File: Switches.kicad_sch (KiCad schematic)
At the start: 114 parts, among them SW1 Esc, SW10 F9, SW100 RightGUI, SW101 App, SW102 RCtrl, SW103 LeftArr, SW104 DownArr, SW105 RightArr, SW106 NP0, SW107 NP., SW108 LCtrl, SW109 LeftGUI, SW11 F10, SW110 Alt, SW111 Space, SW112 Alt Gr, SW113 App, SW114 RCtrl, SW12 F11, SW13 F12, SW14 PrtSc, SW15 ScrLck, SW16 Pause, SW17 `, SW18 1, SW19 2, SW2 F1, SW20 3, SW21 4, SW22 5, SW23 6, SW24 7, SW25 8, SW26 9, SW27 0, SW28 -, SW29 =, SW3 F2, SW30 Bkspc, SW31 Insert, SW32 Home, SW33 PgUp, SW34 NumLck, SW35 NP/, SW36 NP*, SW37 NP-, SW38 Tab, SW39 Q, SW4 F3, SW40 W, SW41 E, SW42 R, SW43 T, SW44 Y, SW45 U, SW46 I, SW47 O, SW48 P, SW49 [, SW5 F4, SW50 ], SW51 ANSI \, SW52 Delete, SW53 End, SW54 PgDn, SW55 NP7, SW56 NP8, SW57 NP9, SW58 NP+, SW59 Caps, SW6 F5, SW60 A, SW61 S, SW62 D, SW63 F, SW64 G, SW65 H, SW66 J, SW67 K, SW68 L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

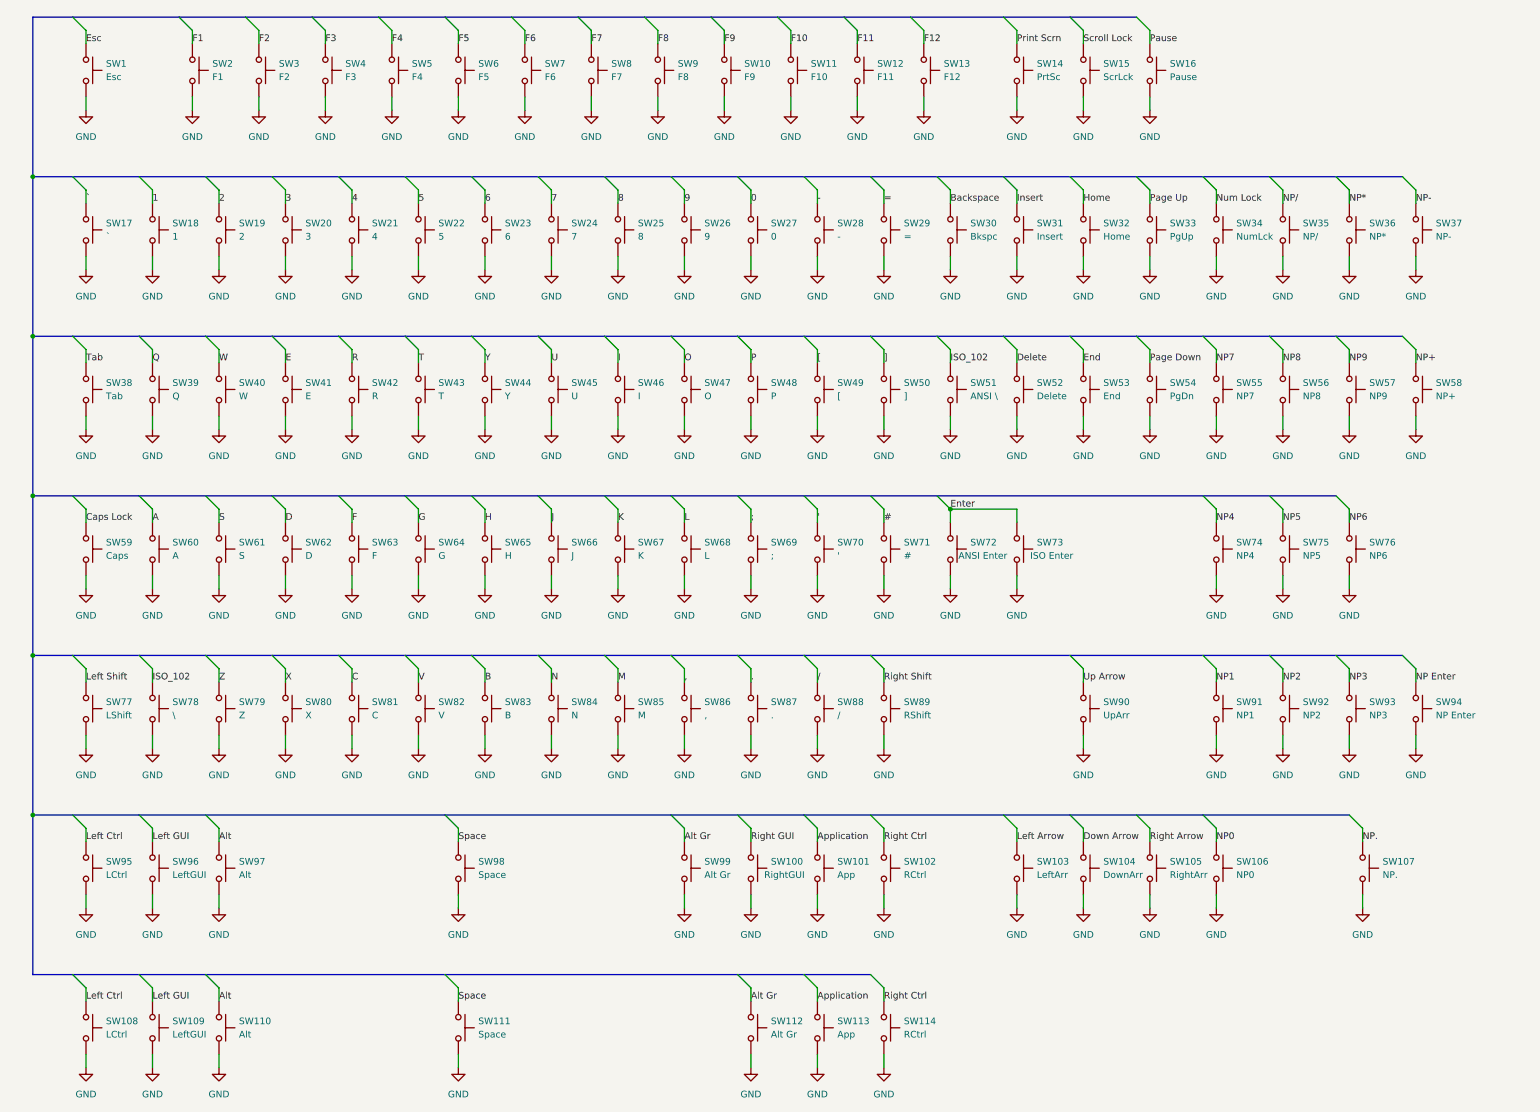
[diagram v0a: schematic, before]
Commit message: updates to board-to-board connector placement
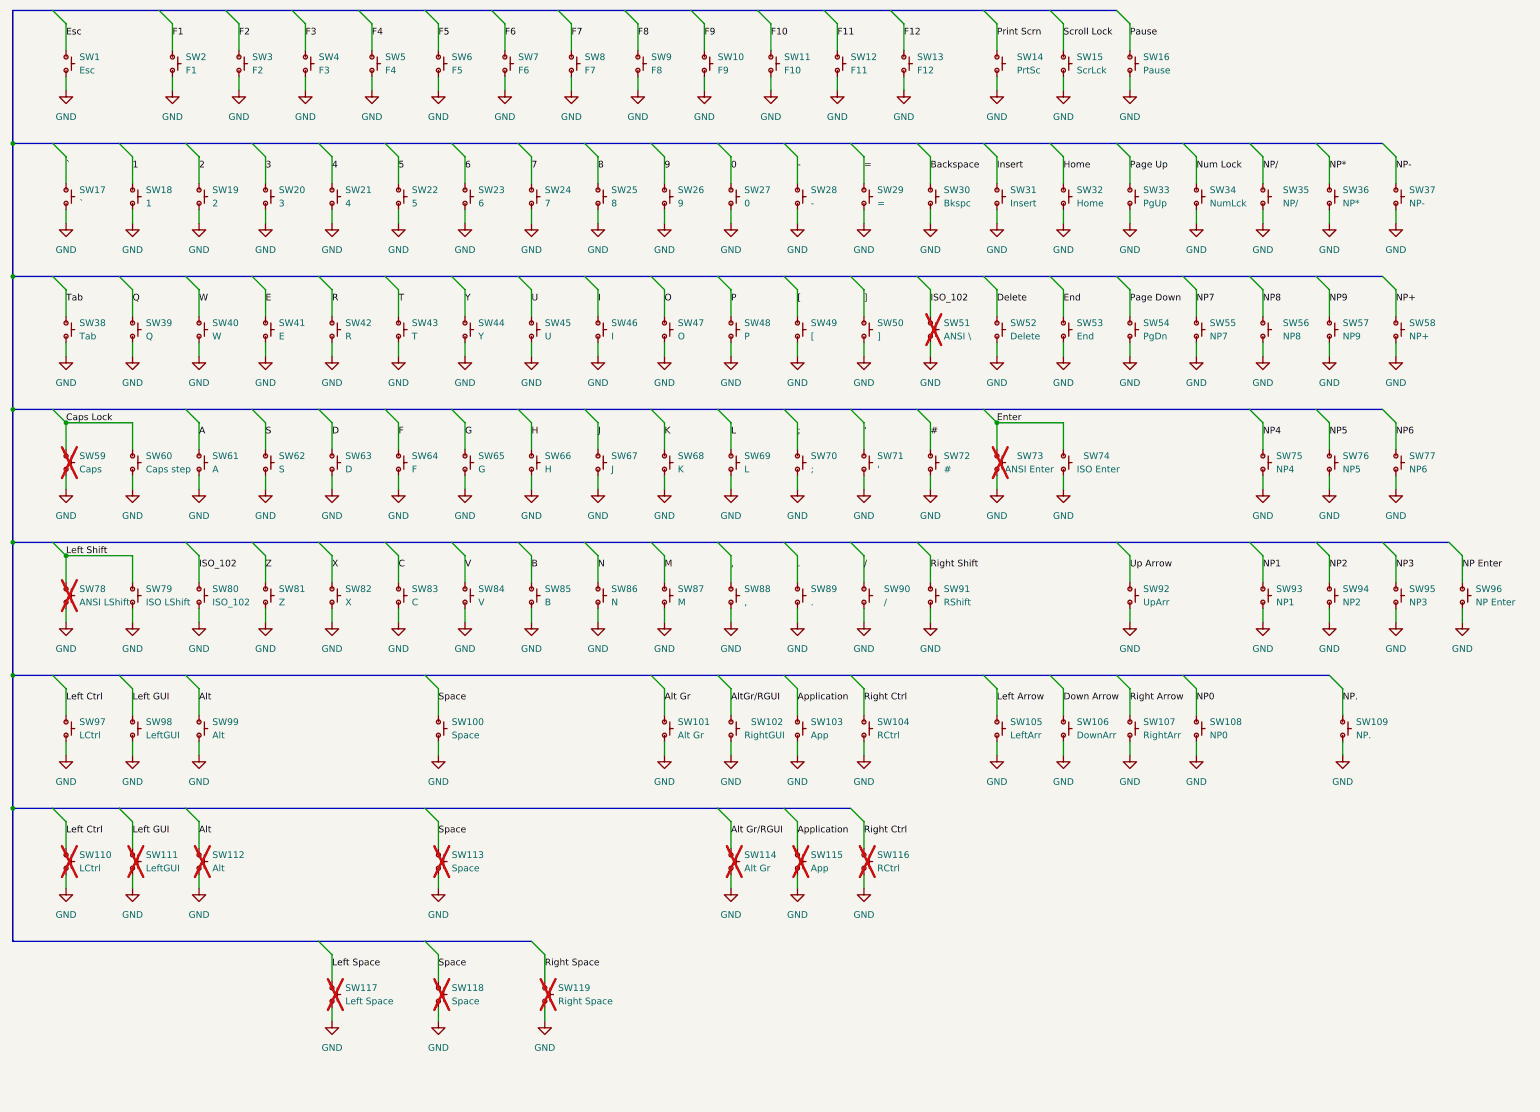
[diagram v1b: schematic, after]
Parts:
- added SW117: Left Space, Switches_Keyboard:SW_Cherry_MX_Convex_2.75u_PCB, symbol Switches_Keyboard:SW-KB-Convex_2.75u-Hot_swap_capable-CherryMX
- added SW118: Space, Switches_Keyboard:SW_Cherry_MX_Convex_1.00u_PCB, symbol Switches_Keyboard:SW-KB-Convex_1.00u-Hot_swap_capable-CherryMX
- added SW119: Right Space, Switches_Keyboard:SW_Cherry_MX_Convex_2.25u_PCB, symbol Switches_Keyboard:SW-KB-Convex_2.25u-Hot_swap_capable-CherryMX
- added SW60: Caps step, Switches_Keyboard:SW_Cherry_MX_R3_1.75u_PCB, symbol Switches_Keyboard:SW-KB-R3_1.75u-Hot_swap_capable-CherryMX
- added SW78: ANSI LShift, Switches_Keyboard:SW_Cherry_MX_R4_2.25u_PCB, symbol Switches_Keyboard:SW-KB-R4_2.25u-Hot_swap_capable-CherryMX
- SW1, SW10, SW11, SW12, SW13, SW14, SW15, SW16, SW17, SW18, SW19, SW2, SW20, SW21, SW22, SW23, SW24, SW25, SW26, SW27, SW28, SW29, SW3, SW31, SW32, SW33, SW34, SW35, SW36, SW37, SW4, SW5, SW6, SW7, SW8, SW9: footprint (none) -> Switches_Keyboard:SW_Cherry_MX_R1_1.00u_PCB; symbol Switch:SW_Push -> Switches_Keyboard:SW-KB-R1_1.00u-Hot_swap_capable-CherryMX; Manufacturer (none) -> Chosen by user; Mfr. Part Number (none) -> Chosen by user
- SW100: renamed from SW98; footprint (none) -> Switches_Keyboard:SW_Cherry_MX_Convex_6.25u_PCB; symbol Switch:SW_Push -> Switches_Keyboard:SW-KB-Convex_6.25u-Hot_swap_capable-CherryMX; Manufacturer (none) -> Chosen by user; Mfr. Part Number (none) -> Chosen by user
- SW101: renamed from SW99; footprint (none) -> Switches_Keyboard:SW_Cherry_MX_R4_1.25u_PCB; symbol Switch:SW_Push -> Switches_Keyboard:SW-KB-R4_1.25u-Hot_swap_capable-CherryMX; Manufacturer (none) -> Chosen by user; Mfr. Part Number (none) -> Chosen by user
- SW102: renamed from SW100; footprint (none) -> Switches_Keyboard:SW_Cherry_MX_R4_1.25u_PCB; symbol Switch:SW_Push -> Switches_Keyboard:SW-KB-R4_1.25u-Hot_swap_capable-CherryMX; Manufacturer (none) -> Chosen by user; Mfr. Part Number (none) -> Chosen by user
- SW103: renamed from SW101; footprint (none) -> Switches_Keyboard:SW_Cherry_MX_R4_1.25u_PCB; symbol Switch:SW_Push -> Switches_Keyboard:SW-KB-R4_1.25u-Hot_swap_capable-CherryMX; Manufacturer (none) -> Chosen by user; Mfr. Part Number (none) -> Chosen by user
- SW104: renamed from SW102; footprint (none) -> Switches_Keyboard:SW_Cherry_MX_R4_1.25u_PCB; symbol Switch:SW_Push -> Switches_Keyboard:SW-KB-R4_1.25u-Hot_swap_capable-CherryMX; Manufacturer (none) -> Chosen by user; Mfr. Part Number (none) -> Chosen by user
- SW105: renamed from SW103; footprint (none) -> Switches_Keyboard:SW_Cherry_MX_R4_1.00u_PCB; symbol Switch:SW_Push -> Switches_Keyboard:SW-KB-R4_1.00u-Hot_swap_capable-CherryMX; Manufacturer (none) -> Chosen by user; Mfr. Part Number (none) -> Chosen by user
- SW106: renamed from SW104; footprint (none) -> Switches_Keyboard:SW_Cherry_MX_R4_1.00u_PCB; symbol Switch:SW_Push -> Switches_Keyboard:SW-KB-R4_1.00u-Hot_swap_capable-CherryMX; Manufacturer (none) -> Chosen by user; Mfr. Part Number (none) -> Chosen by user
- SW107: renamed from SW105; footprint (none) -> Switches_Keyboard:SW_Cherry_MX_R4_1.00u_PCB; symbol Switch:SW_Push -> Switches_Keyboard:SW-KB-R4_1.00u-Hot_swap_capable-CherryMX; Manufacturer (none) -> Chosen by user; Mfr. Part Number (none) -> Chosen by user
- SW108: renamed from SW106; footprint (none) -> Switches_Keyboard:SW_Cherry_MX_R4_2.00u_PCB; symbol Switch:SW_Push -> Switches_Keyboard:SW-KB-R4_2.00u-Hot_swap_capable-CherryMX; Manufacturer (none) -> Chosen by user; Mfr. Part Number (none) -> Chosen by user
- SW109: renamed from SW107; footprint (none) -> Switches_Keyboard:SW_Cherry_MX_R4_1.00u_PCB; symbol Switch:SW_Push -> Switches_Keyboard:SW-KB-R4_1.00u-Hot_swap_capable-CherryMX; Manufacturer (none) -> Chosen by user; Mfr. Part Number (none) -> Chosen by user
- SW110: renamed from SW108; footprint (none) -> Switches_Keyboard:SW_Cherry_MX_R4_1.50u_PCB; symbol Switch:SW_Push -> Switches_Keyboard:SW-KB-R4_1.50u-Hot_swap_capable-CherryMX; Manufacturer (none) -> Chosen by user; Mfr. Part Number (none) -> Chosen by user; now not fitted
- SW111: renamed from SW109; footprint (none) -> Switches_Keyboard:SW_Cherry_MX_R4_1.00u_PCB; symbol Switch:SW_Push -> Switches_Keyboard:SW-KB-R4_1.00u-Hot_swap_capable-CherryMX; Manufacturer (none) -> Chosen by user; Mfr. Part Number (none) -> Chosen by user; now not fitted
- SW112: renamed from SW110; footprint (none) -> Switches_Keyboard:SW_Cherry_MX_R4_1.50u_PCB; symbol Switch:SW_Push -> Switches_Keyboard:SW-KB-R4_1.50u-Hot_swap_capable-CherryMX; Manufacturer (none) -> Chosen by user; Mfr. Part Number (none) -> Chosen by user; now not fitted
- SW113: renamed from SW111; footprint (none) -> Switches_Keyboard:SW_Cherry_MX_Convex_7.00u_PCB; symbol Switch:SW_Push -> Switches_Keyboard:SW-KB-Convex_7.00u-Hot_swap_capable-CherryMX; Manufacturer (none) -> Chosen by user; Mfr. Part Number (none) -> Chosen by user; now not fitted
- SW114: renamed from SW112; footprint (none) -> Switches_Keyboard:SW_Cherry_MX_R4_1.50u_PCB; symbol Switch:SW_Push -> Switches_Keyboard:SW-KB-R4_1.50u-Hot_swap_capable-CherryMX; Manufacturer (none) -> Chosen by user; Mfr. Part Number (none) -> Chosen by user; now not fitted
- SW115: renamed from SW113; footprint (none) -> Switches_Keyboard:SW_Cherry_MX_R4_1.00u_PCB; symbol Switch:SW_Push -> Switches_Keyboard:SW-KB-R4_1.00u-Hot_swap_capable-CherryMX; Manufacturer (none) -> Chosen by user; Mfr. Part Number (none) -> Chosen by user; now not fitted
- SW116: renamed from SW114; footprint (none) -> Switches_Keyboard:SW_Cherry_MX_R4_1.50u_PCB; symbol Switch:SW_Push -> Switches_Keyboard:SW-KB-R4_1.50u-Hot_swap_capable-CherryMX; Manufacturer (none) -> Chosen by user; Mfr. Part Number (none) -> Chosen by user; now not fitted
- SW30: footprint (none) -> Switches_Keyboard:SW_Cherry_MX_R1_2.00u_PCB; symbol Switch:SW_Push -> Switches_Keyboard:SW-KB-R1_2.00u-Hot_swap_capable-CherryMX; Manufacturer (none) -> Chosen by user; Mfr. Part Number (none) -> Chosen by user
- SW38: footprint (none) -> Switches_Keyboard:SW_Cherry_MX_R2_1.50u_PCB; symbol Switch:SW_Push -> Switches_Keyboard:SW-KB-R2_1.50u-Hot_swap_capable-CherryMX; Manufacturer (none) -> Chosen by user; Mfr. Part Number (none) -> Chosen by user
- SW39, SW40, SW41, SW42, SW43, SW44, SW45, SW46, SW47, SW48, SW49, SW50, SW52, SW53, SW54, SW55, SW56, SW57: footprint (none) -> Switches_Keyboard:SW_Cherry_MX_R2_1.00u_PCB; symbol Switch:SW_Push -> Switches_Keyboard:SW-KB-R2_1.00u-Hot_swap_capable-CherryMX; Manufacturer (none) -> Chosen by user; Mfr. Part Number (none) -> Chosen by user
- SW51: footprint (none) -> Switches_Keyboard:SW_Cherry_MX_R2_1.50u_PCB; symbol Switch:SW_Push -> Switches_Keyboard:SW-KB-R2_1.50u-Hot_swap_capable-CherryMX; Manufacturer (none) -> Chosen by user; Mfr. Part Number (none) -> Chosen by user; now not fitted
- SW58: footprint (none) -> Switches_Keyboard:SW_Cherry_MX_R2-R3_1.00u_PCB; symbol Switch:SW_Push -> Switches_Keyboard:SW-KB-R2_R3_1.00u-Hot_swap_capable-CherryMX; Manufacturer (none) -> Chosen by user; Mfr. Part Number (none) -> Chosen by user
- SW59: footprint (none) -> Switches_Keyboard:SW_Cherry_MX_R3_1.75u_Stepped_PCB; symbol Switch:SW_Push -> Switches_Keyboard:SW-KB-R3_1.75u_Stepped-Hot_swap_capable-CherryMX; Manufacturer (none) -> Chosen by user; Mfr. Part Number (none) -> Chosen by user; now not fitted
- SW61: renamed from SW60; footprint (none) -> Switches_Keyboard:SW_Cherry_MX_R3_1.00u_PCB; symbol Switch:SW_Push -> Switches_Keyboard:SW-KB-R3_1.00u-Hot_swap_capable-CherryMX; Manufacturer (none) -> Chosen by user; Mfr. Part Number (none) -> Chosen by user
- SW62: renamed from SW61; footprint (none) -> Switches_Keyboard:SW_Cherry_MX_R3_1.00u_PCB; symbol Switch:SW_Push -> Switches_Keyboard:SW-KB-R3_1.00u-Hot_swap_capable-CherryMX; Manufacturer (none) -> Chosen by user; Mfr. Part Number (none) -> Chosen by user
- SW63: renamed from SW62; footprint (none) -> Switches_Keyboard:SW_Cherry_MX_R3_1.00u_PCB; symbol Switch:SW_Push -> Switches_Keyboard:SW-KB-R3_1.00u-Hot_swap_capable-CherryMX; Manufacturer (none) -> Chosen by user; Mfr. Part Number (none) -> Chosen by user
- SW64: renamed from SW63; footprint (none) -> Switches_Keyboard:SW_Cherry_MX_R3_1.00u_PCB; symbol Switch:SW_Push -> Switches_Keyboard:SW-KB-R3_1.00u-Hot_swap_capable-CherryMX; Manufacturer (none) -> Chosen by user; Mfr. Part Number (none) -> Chosen by user
- SW65: renamed from SW64; footprint (none) -> Switches_Keyboard:SW_Cherry_MX_R3_1.00u_PCB; symbol Switch:SW_Push -> Switches_Keyboard:SW-KB-R3_1.00u-Hot_swap_capable-CherryMX; Manufacturer (none) -> Chosen by user; Mfr. Part Number (none) -> Chosen by user
- SW66: renamed from SW65; footprint (none) -> Switches_Keyboard:SW_Cherry_MX_R3_1.00u_PCB; symbol Switch:SW_Push -> Switches_Keyboard:SW-KB-R3_1.00u-Hot_swap_capable-CherryMX; Manufacturer (none) -> Chosen by user; Mfr. Part Number (none) -> Chosen by user
- SW67: renamed from SW66; footprint (none) -> Switches_Keyboard:SW_Cherry_MX_R3_1.00u_PCB; symbol Switch:SW_Push -> Switches_Keyboard:SW-KB-R3_1.00u-Hot_swap_capable-CherryMX; Manufacturer (none) -> Chosen by user; Mfr. Part Number (none) -> Chosen by user
- SW68: renamed from SW67; footprint (none) -> Switches_Keyboard:SW_Cherry_MX_R3_1.00u_PCB; symbol Switch:SW_Push -> Switches_Keyboard:SW-KB-R3_1.00u-Hot_swap_capable-CherryMX; Manufacturer (none) -> Chosen by user; Mfr. Part Number (none) -> Chosen by user
- SW69: renamed from SW68; footprint (none) -> Switches_Keyboard:SW_Cherry_MX_R3_1.00u_PCB; symbol Switch:SW_Push -> Switches_Keyboard:SW-KB-R3_1.00u-Hot_swap_capable-CherryMX; Manufacturer (none) -> Chosen by user; Mfr. Part Number (none) -> Chosen by user
- SW70: renamed from SW69; footprint (none) -> Switches_Keyboard:SW_Cherry_MX_R3_1.00u_PCB; symbol Switch:SW_Push -> Switches_Keyboard:SW-KB-R3_1.00u-Hot_swap_capable-CherryMX; Manufacturer (none) -> Chosen by user; Mfr. Part Number (none) -> Chosen by user
- SW71: renamed from SW70; footprint (none) -> Switches_Keyboard:SW_Cherry_MX_R3_1.00u_PCB; symbol Switch:SW_Push -> Switches_Keyboard:SW-KB-R3_1.00u-Hot_swap_capable-CherryMX; Manufacturer (none) -> Chosen by user; Mfr. Part Number (none) -> Chosen by user
- SW72: renamed from SW71; footprint (none) -> Switches_Keyboard:SW_Cherry_MX_R3_1.00u_PCB; symbol Switch:SW_Push -> Switches_Keyboard:SW-KB-R3_1.00u-Hot_swap_capable-CherryMX; Manufacturer (none) -> Chosen by user; Mfr. Part Number (none) -> Chosen by user
- SW73: renamed from SW72; footprint (none) -> Switches_Keyboard:SW_Cherry_MX_R3_2.25u_PCB; symbol Switch:SW_Push -> Switches_Keyboard:SW-KB-R3_2.25u-Hot_swap_capable-CherryMX; Manufacturer (none) -> Chosen by user; Mfr. Part Number (none) -> Chosen by user; now not fitted
- SW74: renamed from SW73; footprint (none) -> Switches_Keyboard:SW_Cherry_MX_ISO_Enter_PCB; symbol Switch:SW_Push -> Switches_Keyboard:SW-KB-ISO_Enter-Hot_swap_capable-CherryMX; Manufacturer (none) -> Chosen by user; Mfr. Part Number (none) -> Chosen by user
- SW75: renamed from SW74; footprint (none) -> Switches_Keyboard:SW_Cherry_MX_R3_1.00u_PCB; symbol Switch:SW_Push -> Switches_Keyboard:SW-KB-R3_1.00u-Hot_swap_capable-CherryMX; Manufacturer (none) -> Chosen by user; Mfr. Part Number (none) -> Chosen by user
- SW76: renamed from SW75; footprint (none) -> Switches_Keyboard:SW_Cherry_MX_R3_1.00u_PCB; symbol Switch:SW_Push -> Switches_Keyboard:SW-KB-R3_1.00u-Hot_swap_capable-CherryMX; Manufacturer (none) -> Chosen by user; Mfr. Part Number (none) -> Chosen by user
- SW77: renamed from SW76; footprint (none) -> Switches_Keyboard:SW_Cherry_MX_R3_1.00u_PCB; symbol Switch:SW_Push -> Switches_Keyboard:SW-KB-R3_1.00u-Hot_swap_capable-CherryMX; Manufacturer (none) -> Chosen by user; Mfr. Part Number (none) -> Chosen by user
- SW79: renamed from SW77; value LShift -> ISO LShift; footprint (none) -> Switches_Keyboard:SW_Cherry_MX_R4_1.25u_PCB; symbol Switch:SW_Push -> Switches_Keyboard:SW-KB-R4_1.25u-Hot_swap_capable-CherryMX; Manufacturer (none) -> Chosen by user; Mfr. Part Number (none) -> Chosen by user
- SW80: renamed from SW78; value \ -> ISO_102; footprint (none) -> Switches_Keyboard:SW_Cherry_MX_R4_1.00u_PCB; symbol Switch:SW_Push -> Switches_Keyboard:SW-KB-R4_1.00u-Hot_swap_capable-CherryMX; Manufacturer (none) -> Chosen by user; Mfr. Part Number (none) -> Chosen by user
- SW81: renamed from SW79; footprint (none) -> Switches_Keyboard:SW_Cherry_MX_R4_1.00u_PCB; symbol Switch:SW_Push -> Switches_Keyboard:SW-KB-R4_1.00u-Hot_swap_capable-CherryMX; Manufacturer (none) -> Chosen by user; Mfr. Part Number (none) -> Chosen by user
- SW82: renamed from SW80; footprint (none) -> Switches_Keyboard:SW_Cherry_MX_R4_1.00u_PCB; symbol Switch:SW_Push -> Switches_Keyboard:SW-KB-R4_1.00u-Hot_swap_capable-CherryMX; Manufacturer (none) -> Chosen by user; Mfr. Part Number (none) -> Chosen by user
- SW83: renamed from SW81; footprint (none) -> Switches_Keyboard:SW_Cherry_MX_R4_1.00u_PCB; symbol Switch:SW_Push -> Switches_Keyboard:SW-KB-R4_1.00u-Hot_swap_capable-CherryMX; Manufacturer (none) -> Chosen by user; Mfr. Part Number (none) -> Chosen by user
- SW84: renamed from SW82; footprint (none) -> Switches_Keyboard:SW_Cherry_MX_R4_1.00u_PCB; symbol Switch:SW_Push -> Switches_Keyboard:SW-KB-R4_1.00u-Hot_swap_capable-CherryMX; Manufacturer (none) -> Chosen by user; Mfr. Part Number (none) -> Chosen by user
- SW85: renamed from SW83; footprint (none) -> Switches_Keyboard:SW_Cherry_MX_R4_1.00u_PCB; symbol Switch:SW_Push -> Switches_Keyboard:SW-KB-R4_1.00u-Hot_swap_capable-CherryMX; Manufacturer (none) -> Chosen by user; Mfr. Part Number (none) -> Chosen by user
- SW86: renamed from SW84; footprint (none) -> Switches_Keyboard:SW_Cherry_MX_R4_1.00u_PCB; symbol Switch:SW_Push -> Switches_Keyboard:SW-KB-R4_1.00u-Hot_swap_capable-CherryMX; Manufacturer (none) -> Chosen by user; Mfr. Part Number (none) -> Chosen by user
- SW87: renamed from SW85; footprint (none) -> Switches_Keyboard:SW_Cherry_MX_R4_1.00u_PCB; symbol Switch:SW_Push -> Switches_Keyboard:SW-KB-R4_1.00u-Hot_swap_capable-CherryMX; Manufacturer (none) -> Chosen by user; Mfr. Part Number (none) -> Chosen by user
- SW88: renamed from SW86; footprint (none) -> Switches_Keyboard:SW_Cherry_MX_R4_1.00u_PCB; symbol Switch:SW_Push -> Switches_Keyboard:SW-KB-R4_1.00u-Hot_swap_capable-CherryMX; Manufacturer (none) -> Chosen by user; Mfr. Part Number (none) -> Chosen by user
- SW89: renamed from SW87; footprint (none) -> Switches_Keyboard:SW_Cherry_MX_R4_1.00u_PCB; symbol Switch:SW_Push -> Switches_Keyboard:SW-KB-R4_1.00u-Hot_swap_capable-CherryMX; Manufacturer (none) -> Chosen by user; Mfr. Part Number (none) -> Chosen by user
- SW90: renamed from SW88; footprint (none) -> Switches_Keyboard:SW_Cherry_MX_R4_1.00u_PCB; symbol Switch:SW_Push -> Switches_Keyboard:SW-KB-R4_1.00u-Hot_swap_capable-CherryMX; Manufacturer (none) -> Chosen by user; Mfr. Part Number (none) -> Chosen by user
- SW91: renamed from SW89; footprint (none) -> Switches_Keyboard:SW_Cherry_MX_R4_2.75u_PCB; symbol Switch:SW_Push -> Switches_Keyboard:SW-KB-R4_2.75u-Hot_swap_capable-CherryMX; Manufacturer (none) -> Chosen by user; Mfr. Part Number (none) -> Chosen by user
- SW92: renamed from SW90; footprint (none) -> Switches_Keyboard:SW_Cherry_MX_R4_1.00u_PCB; symbol Switch:SW_Push -> Switches_Keyboard:SW-KB-R4_1.00u-Hot_swap_capable-CherryMX; Manufacturer (none) -> Chosen by user; Mfr. Part Number (none) -> Chosen by user
- SW93: renamed from SW91; footprint (none) -> Switches_Keyboard:SW_Cherry_MX_R4_1.00u_PCB; symbol Switch:SW_Push -> Switches_Keyboard:SW-KB-R4_1.00u-Hot_swap_capable-CherryMX; Manufacturer (none) -> Chosen by user; Mfr. Part Number (none) -> Chosen by user
- SW94: renamed from SW92; footprint (none) -> Switches_Keyboard:SW_Cherry_MX_R4_1.00u_PCB; symbol Switch:SW_Push -> Switches_Keyboard:SW-KB-R4_1.00u-Hot_swap_capable-CherryMX; Manufacturer (none) -> Chosen by user; Mfr. Part Number (none) -> Chosen by user
- SW95: renamed from SW93; footprint (none) -> Switches_Keyboard:SW_Cherry_MX_R4_1.00u_PCB; symbol Switch:SW_Push -> Switches_Keyboard:SW-KB-R4_1.00u-Hot_swap_capable-CherryMX; Manufacturer (none) -> Chosen by user; Mfr. Part Number (none) -> Chosen by user
- SW96: renamed from SW94; footprint (none) -> Switches_Keyboard:SW_Cherry_MX_R4-R4_1.00u_PCB; symbol Switch:SW_Push -> Switches_Keyboard:SW-KB-R4_R4_1.00u-Hot_swap_capable-CherryMX; Manufacturer (none) -> Chosen by user; Mfr. Part Number (none) -> Chosen by user
- SW97: renamed from SW95; footprint (none) -> Switches_Keyboard:SW_Cherry_MX_R4_1.25u_PCB; symbol Switch:SW_Push -> Switches_Keyboard:SW-KB-R4_1.25u-Hot_swap_capable-CherryMX; Manufacturer (none) -> Chosen by user; Mfr. Part Number (none) -> Chosen by user
- SW98: renamed from SW96; footprint (none) -> Switches_Keyboard:SW_Cherry_MX_R4_1.25u_PCB; symbol Switch:SW_Push -> Switches_Keyboard:SW-KB-R4_1.25u-Hot_swap_capable-CherryMX; Manufacturer (none) -> Chosen by user; Mfr. Part Number (none) -> Chosen by user
- SW99: renamed from SW97; footprint (none) -> Switches_Keyboard:SW_Cherry_MX_R4_1.25u_PCB; symbol Switch:SW_Push -> Switches_Keyboard:SW-KB-R4_1.25u-Hot_swap_capable-CherryMX; Manufacturer (none) -> Chosen by user; Mfr. Part Number (none) -> Chosen by user
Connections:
- net Alt Gr: no longer SW114.1
- net Caps Lock: now also SW60.1
- net GND: now also SW117.2, SW118.2, SW119.2, SW60.2, SW78.2
- net Left Shift: now also SW78.1
- net Space: now also SW118.1
- net Right GUI renamed AltGr/RGUI
- new net Alt Gr/RGUI: SW114.1
- new net Left Space: SW117.1
- new net Right Space: SW119.1
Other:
- company: (none) -> Egill Milan Gunnarsson
- title: (none) -> KB01
- moved on the sheet: SW1, SW10, SW100, SW101, SW102, SW103, SW104, SW105, SW106, SW107, SW108, SW109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
